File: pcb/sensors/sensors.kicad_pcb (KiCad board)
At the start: 2 copper layers, 48 parts, among them J1 POWER / 5V RECOM, J2 USB-C FLASH, J3 CAN BUS, J4 DIMMER / GROVE, J5 XDB401 / GROVE, J6 DIGMESA / FLOW, J7 M5STACK VALVE SSR, J8 BOILER SSR / 5V OUT, Q2 AO3401A, Q3 2N7002, SW1 BOOT, SW2 RESET, U1 ESP32-S3-MINI-1U-N8, U2 AMS1117-3.3, U4 TJA1051T/3, U5 TMP102AIDRLR

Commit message: pcb sensors: update
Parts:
- removed JP1: CAN TERM, Connector_PinHeader_2.54mm:PinHeader_1x02_P2.54mm_Vertical
- removed R1: 270, Resistor_SMD:R_0603_1608Metric
- AMS1117: renamed from U2; value AMS1117-3.3 -> AMS1117
- J1: value POWER / 5V RECOM -> POWER 5V
- R12: value 120 / 0.25W -> 120
- U1: value ESP32-S3-MINI-1U-N8 -> ESP32-S3
- U5: value TMP102AIDRLR -> TMP102
- moved R17 58.2 mm to (62.5, 95.9)
- moved SW1 49.5 mm to (89.7, 58.6)
- moved C10 47.2 mm to (108.0, 70.0)
- moved R3 46.8 mm to (84.5, 57.7), turned to 90 degrees
- moved C4 41.6 mm to (84.0, 65.0), turned to 90 degrees
- moved C5 40.8 mm to (86.0, 64.8), turned to 90 degrees
- moved C13 37.5 mm to (59.0, 74.4)
- moved C8 34.3 mm to (82.7, 70.5)
- moved R11 34.2 mm to (82.5, 74.5)
- moved R12 28.8 mm to (69.0, 73.0), turned to 90 degrees
- moved C9 27.3 mm to (71.5, 69.0)
- moved C12 26.8 mm to (64.3, 75.9)
- moved J6 26.6 mm to (58.0, 80.7)
- moved J7 26.6 mm to (58.0, 88.5)
- moved C2 25.0 mm to (93.3, 79.5)
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- renumbered U4 to TJA1051
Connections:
- R12 pad 1: /Sensors interfaces/CAN_TERM -> /Sensors interfaces/CAN_H

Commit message: manual PCB design
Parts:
- removed AMS1117: AMS1117, Package_TO_SOT_SMD:SOT-223-3_TabPin2
- removed C11, C13: 100nF, Capacitor_SMD:C_0603_1608Metric
- removed J5: XDB401 / GROVE, Connector:NS-Tech_Grove_1x04_P2mm_Vertical
- removed SW1: BOOT, Button_Switch_SMD:SW_SPST_TL3342
- removed SW2: RESET, Button_Switch_SMD:SW_SPST_TL3342
- removed TJA1051: TJA1051T/3, Package_SO:SOIC-8_3.9x4.9mm_P1.27mm
- added ?: M2, MountingHole:MountingHole_2.2mm_M2_ISO7380, F.Cu at (186.0, 148.0)
- added ?: M2, MountingHole:MountingHole_2.2mm_M2_ISO7380, F.Cu at (157.0, 148.0)
- added ?: M2, MountingHole:MountingHole_2.2mm_M2_ISO7380, F.Cu at (157.0, 102.0)
- added ?: M2, MountingHole:MountingHole_2.2mm_M2_ISO7380, F.Cu at (186.0, 102.0)
- added BOOT: BOOT, Button_Switch_SMD:SW_SPST_TS-1088-xR020, F.Cu at (157.5, 139.0)
- added RESET: RESET, Button_Switch_SMD:SW_SPST_TS-1088-xR020, F.Cu at (174.3, 105.0)
- added U2: AMS1117-3.3, Package_TO_SOT_SMD:SOT-223-3_TabPin2, F.Cu at (167.0, 111.5)
- added U4: TJA1051T/3, Package_SO:SOIC-8_3.9x4.9mm_P1.27mm, F.Cu at (161.0, 132.6)
- 5V: renamed from J1; value POWER 5V -> 5V POWER
- BOILER: renamed from J8; value BOILER SSR / 5V OUT -> BOILER SSR
- DIMMER: renamed from J4; value DIMMER / GROVE -> DIMMER I2C
- FLOW: renamed from J6; value DIGMESA / FLOW -> FLOW HALL
- J2: footprint Connector_USB:USB_C_Receptacle_GCT_USB4105-xx-A_16P_TopMnt_Horizontal -> Sensors_Local:USB_C_Receptacle_GCT_USB4105-xx-A_16P_TopMnt_Horizontal_RoundedGND
- R12: value 120 -> 120 / 0.25W
- U1: value ESP32-S3 -> ESP32-S3-MINI-1U-N8
- U5: value TMP102 -> TMP102AIDRLR
- VALVE: renamed from J7; value M5STACK VALVE SSR -> VALVE SSR
- moved C12 130.6 mm to (184.0, 128.2), turned to -90 degrees
- moved R21 129.9 mm to (164.5, 146.8), turned to 90 degrees
- moved VALVE 128.8 mm to (185.0, 110.1), turned to -90 degrees
- moved Q2 128.0 mm to (167.5, 146.4), turned to 90 degrees
- moved R17 126.9 mm to (184.0, 132.5), turned to -90 degrees
- moved BOILER 126.6 mm to (167.5, 139.0), turned to -90 degrees
- moved R22 126.2 mm to (162.5, 142.0), turned to 90 degrees
- moved FLOW 122.6 mm to (177.0, 110.1), turned to -90 degrees
- moved CAN 120.0 mm to (158.0, 125.0)
- moved Q3 118.6 mm to (161.6, 145.5)
- moved R15 118.5 mm to (171.5, 117.3)
- moved R19 114.9 mm to (162.5, 139.0), turned to 90 degrees
- moved C9 108.2 mm to (161.5, 129.0)
- moved 5V 106.9 mm to (184.0, 141.5), turned to 90 degrees
- moved R3 104.2 mm to (164.0, 125.0), turned to -90 degrees
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- renumbered J3 to CAN
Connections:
- D1 pad 1: /USB_HOST_DP -> /USB_HOST_DM
- D1 pad 2: /USB_HOST_DM -> /USB_HOST_DP
- U1 pad 11: CAN_TX -> unconnected-(U1-IO7-Pad11)
- U1 pad 12: CAN_RX -> unconnected-(U1-IO8-Pad12)
- U1 pad 13: VALVE_CMD -> unconnected-(U1-IO9-Pad13)
- U1 pad 14: HEATER_CMD -> CAN_RX
- U1 pad 15: unconnected-(U1-IO11-Pad15) -> CAN_TX
- U1 pad 16: unconnected-(U1-IO12-Pad16) -> HEATER_CMD
- U1 pad 32: unconnected-(U1-IO36-Pad32) -> VALVE_CMD
- U1 pad 37: unconnected-(U1-IO41-Pad37) -> FLOW_PULSE
- U1 pad 8: FLOW_PULSE -> unconnected-(U1-IO4-Pad8)
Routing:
- net +5V: track 0.00 -> 96.6 mm
- net +3V3: track 0.00 -> 76.0 mm
- net GND: track 0.00 -> 67.5 mm, vias 0 -> 33
- net I2C_SDA: track 0.00 -> 54.2 mm, vias 0 -> 2
- net I2C_SCL: track 0.00 -> 52.0 mm, vias 0 -> 2
- net FLOW_PULSE: track 0.00 -> 25.6 mm
- net /EN: track 0.00 -> 24.0 mm, vias 0 -> 2
- net VALVE_CMD: track 0.00 -> 20.1 mm
- net /BOOT_N: track 0.00 -> 19.6 mm, vias 0 -> 2
- net /Sensors interfaces/CAN_H: track 0.00 -> 17.2 mm
- net /Sensors interfaces/CAN_L: track 0.00 -> 15.5 mm
- net HEATER_CMD: track 0.00 -> 14.9 mm
- net /Sensors interfaces/BOILER_5V: track 0.00 -> 9.80 mm
- net CAN_TX: track 0.00 -> 9.25 mm, vias 0 -> 2
- net /USB_HOST_DP: track 2.90 -> 8.68 mm
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- added copper zone on F.Cu, net +3V3
- added copper zone on B.Cu, net GND
- added copper zone on F.Cu, net GND
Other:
- board outline added: 33 x 50 mm

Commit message: Finalize sensors PCB and JLCPCB manufacturing exports
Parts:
- added D2: GREEN / STATUS, LED_SMD:LED_0603_1608Metric, F.Cu at (179.6, 136.0)
- added R25: 1k, Resistor_SMD:R_0603_1608Metric, F.Cu at (184.8, 130.5)
- I2C: renamed from DIMMER; footprint Connector:NS-Tech_Grove_1x04_P2mm_Vertical -> Sensors_Local:CONN-TH_HY-4A
- moved R2 4.18 mm to (179.2, 104.5), turned to 180 degrees
- moved I2C 0.50 mm to (158.0, 107.0)
- moved R17 0.50 mm to (184.0, 133.0)
- moved R3 0.50 mm to (164.0, 125.5), turned to 0 degrees
- moved R15 0.22 mm to (171.5, 117.1)
- moved C2 0.05 mm to (171.8, 113.7)
- gave numbers to parts that had none: 4
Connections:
- U1 pad 34: unconnected-(U1-IO38-Pad34) -> /STATUS_LED
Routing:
- net /STATUS_LED_A: track 0.00 -> 9.47 mm
- net GND: track 67.5 -> 76.3 mm, vias 33 -> 37
- net +5V: track 96.6 -> 99.1 mm
- net /STATUS_LED: track 0.00 -> 2.17 mm
- net I2C_SDA: track 54.2 -> 55.8 mm
- net /EN: track 24.0 -> 22.4 mm
- net /BOOT_N: track 19.6 -> 18.6 mm
- net VALVE_CMD: track 20.1 -> 20.8 mm
- net +3V3: track 76.0 -> 76.6 mm
- net I2C_SCL: track 52.0 -> 52.6 mm

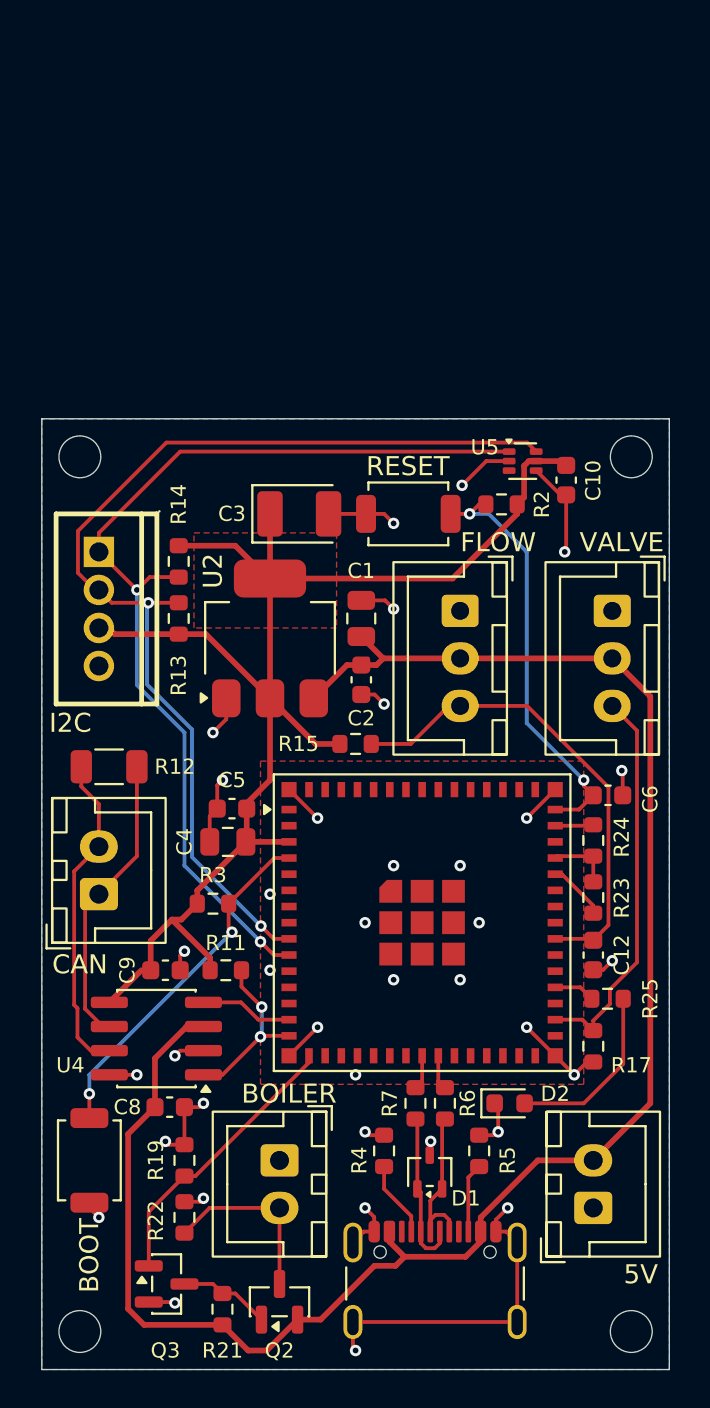
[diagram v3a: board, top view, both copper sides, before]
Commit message: Add Grove I2C passthrough board and update sensors manufacturing
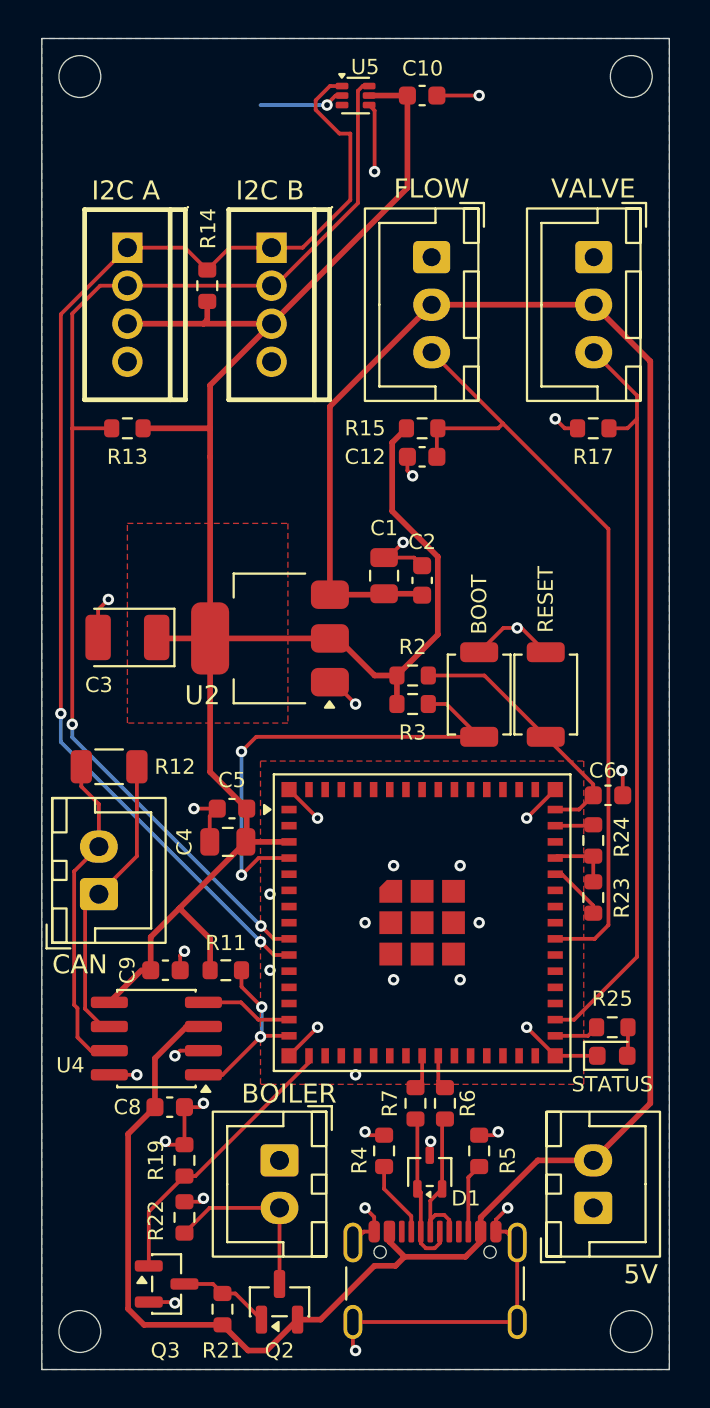
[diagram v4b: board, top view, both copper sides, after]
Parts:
- added I2C A: DIMMER I2C, Sensors_Local:CONN-TH_HY-4A, F.Cu at (159.5, 91.0)
- I2C B: renamed from I2C
- moved R17 32.5 mm to (184.0, 100.5), turned to 180 degrees
- moved BOOT 31.9 mm to (178.0, 114.5), turned to 90 degrees
- moved C12 27.7 mm to (175.0, 102.0), turned to 180 degrees
- moved C10 21.6 mm to (175.0, 83.0), turned to 0 degrees
- moved U5 21.1 mm to (171.5, 83.0)
- moved MH2 20.0 mm to (157.0, 82.0)
- moved MH3 20.0 mm to (186.0, 82.0)
- moved FLOW 18.7 mm to (175.5, 91.5)
- moved VALVE 18.6 mm to (184.0, 91.5)
- moved I2C B 18.4 mm to (167.1, 91.0)
- moved R15 17.0 mm to (175.0, 100.5)
- moved R3 14.8 mm to (174.5, 115.0)
- moved R14 14.6 mm to (163.7, 93.0), turned to 90 degrees
- moved RESET 11.9 mm to (181.5, 114.5), turned to 90 degrees
- moved C3 11.1 mm to (159.5, 111.5), turned to 180 degrees
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- renumbered D2 to STATUS
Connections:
- U1 pad 31: unconnected-(U1-IO35-Pad31) -> /STATUS_LED
- U1 pad 34: /STATUS_LED -> unconnected-(U1-IO38-Pad34)
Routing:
- net +3V3: track 76.6 -> 107.1 mm
- net +5V: track 99.1 -> 129.2 mm
- net VALVE_CMD: track 20.8 -> 40.1 mm
- net FLOW_PULSE: track 25.5 -> 42.1 mm
- net I2C_SCL: track 52.6 -> 65.9 mm
- net /EN: track 22.4 -> 13.9 mm, vias 2 -> 0
- net I2C_SDA: track 55.8 -> 64.2 mm
- net /STATUS_LED_A: track 9.47 -> 1.52 mm
- net /BOOT_N: track 18.6 -> 25.6 mm
- net GND: track 76.3 -> 78.0 mm
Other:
- board size 33 x 50 mm -> 33 x 70 mm

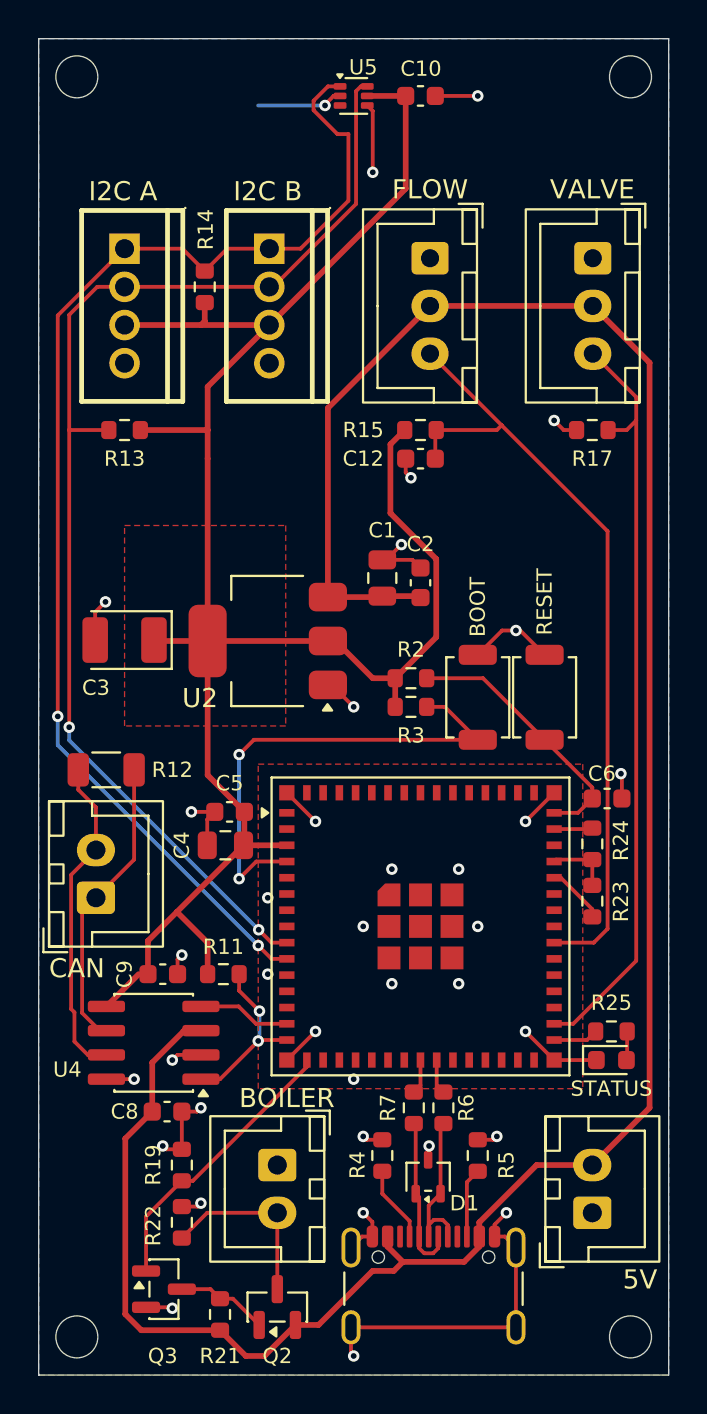
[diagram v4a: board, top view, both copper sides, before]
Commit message: Replace sensors MINI controller with socketed XIAO ESP32-S3
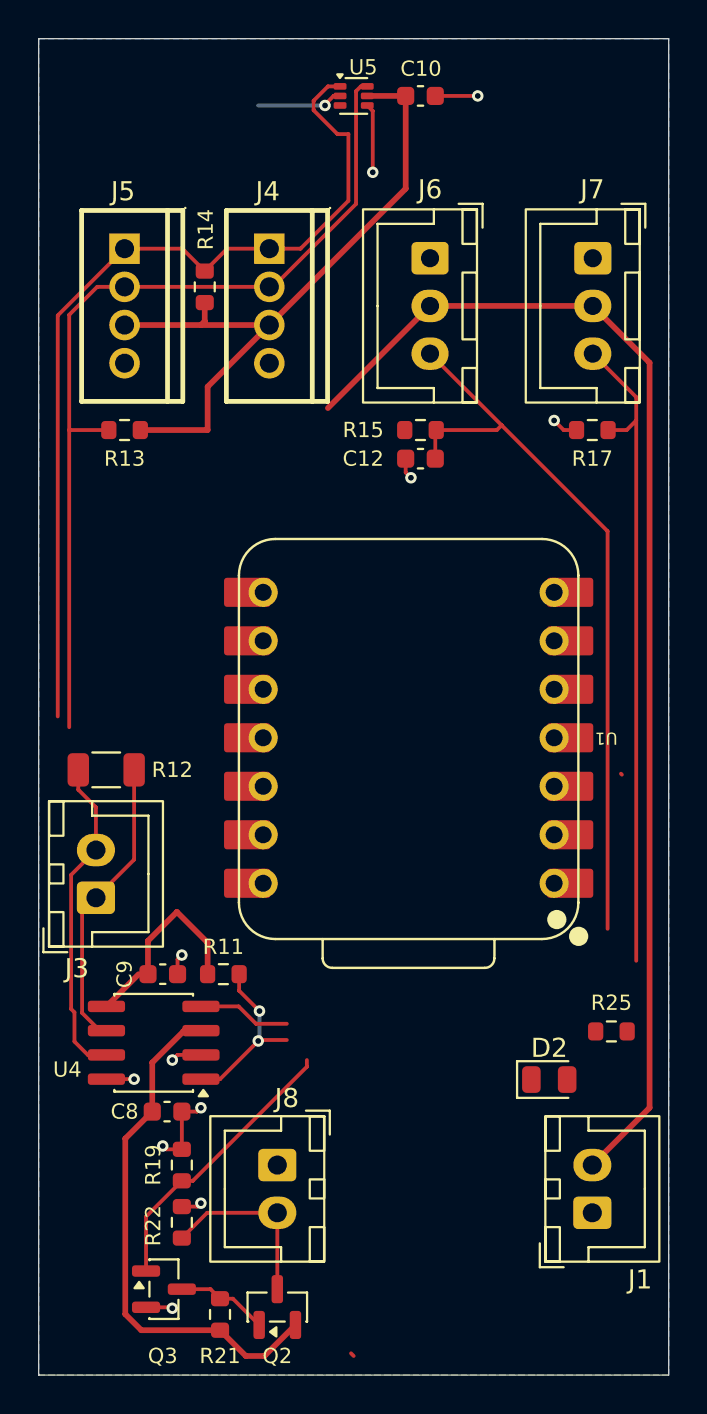
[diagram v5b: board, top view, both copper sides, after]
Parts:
- removed BOOT: BOOT, Button_Switch_SMD:SW_SPST_TS-1088-xR020
- removed C1: 4.7uF, Capacitor_SMD:C_0805_2012Metric
- removed C2, C5: 100nF, Capacitor_SMD:C_0603_1608Metric
- removed C3: 22uF tantalum / 10V, Capacitor_Tantalum_SMD:CP_EIA-3528-21_Kemet-B
- removed C4: 10uF, Capacitor_SMD:C_0805_2012Metric
- removed C6: 1uF, Capacitor_SMD:C_0603_1608Metric
- removed D1: TPD2E2U06DCKR, Package_TO_SOT_SMD:SOT-323_SC-70
- removed J2: USB-C FLASH, Sensors_Local:USB_C_Receptacle_GCT_USB4105-xx-A_16P_TopMnt_Horizontal_RoundedGND
- removed MH1, MH2, MH3, MH4: M2, MountingHole:MountingHole_2.2mm_M2_ISO7380
- removed R2, R23, R24, R3: 10k, Resistor_SMD:R_0603_1608Metric
- removed R4, R5: 5.1k, Resistor_SMD:R_0603_1608Metric
- removed R6, R7: 22, Resistor_SMD:R_0603_1608Metric
- removed RESET: RESET, Button_Switch_SMD:SW_SPST_TS-1088-xR020
- removed STATUS: GREEN / STATUS, LED_SMD:LED_0603_1608Metric
- removed U2: AMS1117-3.3, Package_TO_SOT_SMD:SOT-223-3_TabPin2
- added D2: GREEN / STATUS, LED_SMD:LED_0805_2012Metric, F.Cu at (181.7, 134.5)
- J4: renamed from I2C B
- J5: renamed from I2C A
- U1: value ESP32-S3-MINI-1U-N8 -> XIAO ESP32-S3 / SOCKETED; footprint RF_Module:ESP32-S2-MINI-1U -> Seeed_XIAO:XIAO-ESP32-S3-DIP
- moved U1 9.90 mm to (174.4, 116.6), turned to -90 degrees
- renumbered 5V to J1, CAN to J3, FLOW to J6, VALVE to J7, BOILER to J8
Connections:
- U1 pad 1: GND -> unconnected-(U1-D0-Pad1)
- U1 pad 10: I2C_SCL -> CAN_RX
- U1 pad 11: unconnected-(U1-IO7-Pad11) -> VALVE_CMD
- U1 pad 12: unconnected-(U1-IO8-Pad12) -> +3V3
- U1 pad 13: unconnected-(U1-IO9-Pad13) -> GND
- U1 pad 14: CAN_RX -> +5V
- U1 pad 2: GND -> /STATUS_LED
- U1 pad 3: +3V3 -> unconnected-(U1-D2-Pad3)
- U1 pad 4: /BOOT_N -> HEATER_CMD
- U1 pad 5: unconnected-(U1-IO1-Pad5) -> I2C_SDA
- U1 pad 6: unconnected-(U1-IO2-Pad6) -> I2C_SCL
- U1 pad 8: unconnected-(U1-IO4-Pad8) -> FLOW_PULSE
- U1 pad 9: I2C_SDA -> CAN_TX
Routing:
- net +3V3: track 107.1 -> 46.9 mm
- net GND: track 78.0 -> 23.9 mm, vias 37 -> 12
- net +5V: track 129.2 -> 92.7 mm
- net /BOOT_N: track 25.6 -> 0.00 mm, vias 2 -> 0
- net I2C_SCL: track 65.9 -> 47.7 mm, vias 2 -> 0
- net I2C_SDA: track 64.2 -> 47.7 mm, vias 2 -> 0
- net /EN: track 13.9 -> 0.00 mm
- net /USB_HOST_DP: track 8.68 -> 0.00 mm
- net /USB_HOST_DM: track 8.47 -> 0.00 mm
- net VALVE_CMD: track 40.1 -> 34.4 mm
- net /USB_CC1: track 4.01 -> 0.00 mm
- net /USB_CC2: track 3.66 -> 0.00 mm
- net FLOW_PULSE: track 42.1 -> 39.0 mm
- net /STRAP45: track 3.08 -> 0.00 mm
- net /STATUS_LED: track 2.36 -> 0.00 mm
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- removed copper zone on F.Cu, net +3V3
- removed copper zone on F.Cu, net GND
